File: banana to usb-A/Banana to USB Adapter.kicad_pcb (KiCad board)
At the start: 2 copper layers, 34.3 x 26.6 mm, 9 parts, among them J1 USB_A, J2 Positive, J3 Negative, J4 Data

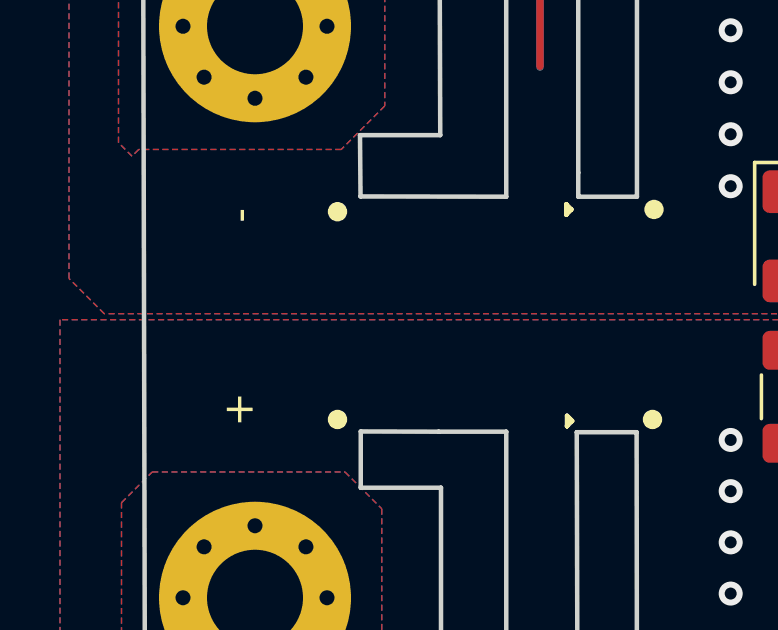
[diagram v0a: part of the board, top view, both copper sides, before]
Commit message: put missing drill holes back! (and locked them
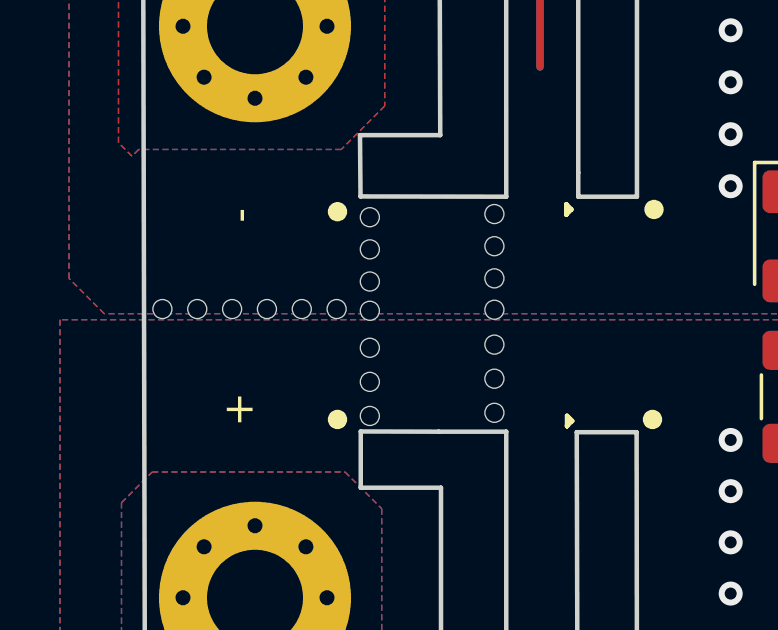
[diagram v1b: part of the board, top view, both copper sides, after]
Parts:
- added ?: , , F.Cu at (137.0, 101.7)
- added ?: , , F.Cu at (137.0, 98.3)
- added ?: , , F.Cu at (137.0, 97.2)
- added ?: , , F.Cu at (137.0, 100.5)
- added ?: , , F.Cu at (137.0, 99.4)
- added ?: , , F.Cu at (137.0, 102.8)
- added ?: , , F.Cu at (137.0, 96.2)
- added REF**: 25mil_Hole, My Libraries:25mil_Hole, F.Cu at (128.4, 99.5)
- added REF**: 25mil_Hole, My Libraries:25mil_Hole, F.Cu at (129.5, 99.5)
- added REF**: 25mil_Hole, My Libraries:25mil_Hole, F.Cu at (133.0, 100.8)
- added REF**: 25mil_Hole, My Libraries:25mil_Hole, F.Cu at (133.0, 96.5)
- added REF**: 25mil_Hole, My Libraries:25mil_Hole, F.Cu at (133.0, 99.6)
- added REF**: 25mil_Hole, My Libraries:25mil_Hole, F.Cu at (126.0, 99.5)
- added REF**: 25mil_Hole, My Libraries:25mil_Hole, F.Cu at (131.8, 99.5)
- added REF**: 25mil_Hole, My Libraries:25mil_Hole, F.Cu at (133.0, 103.1)
- added REF**: 25mil_Hole, My Libraries:25mil_Hole, F.Cu at (130.7, 99.5)
- added REF**: 25mil_Hole, My Libraries:25mil_Hole, F.Cu at (127.2, 99.5)
- added REF**: 25mil_Hole, My Libraries:25mil_Hole, F.Cu at (133.0, 98.6)
- added REF**: 25mil_Hole, My Libraries:25mil_Hole, F.Cu at (133.0, 102.0)
- added REF**: 25mil_Hole, My Libraries:25mil_Hole, F.Cu at (133.0, 97.6)
